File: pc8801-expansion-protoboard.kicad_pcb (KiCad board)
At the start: 2 copper layers, 219 x 95 mm, 42 parts, among them J1 Solder Side, J2 Parts Side, J3 5V, J4 12V, J5 -12V, J6 GND_1, J7 GND_2, U1 ExpansionEdge, U10 74LS165, U11 ESP32-DEVKITC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

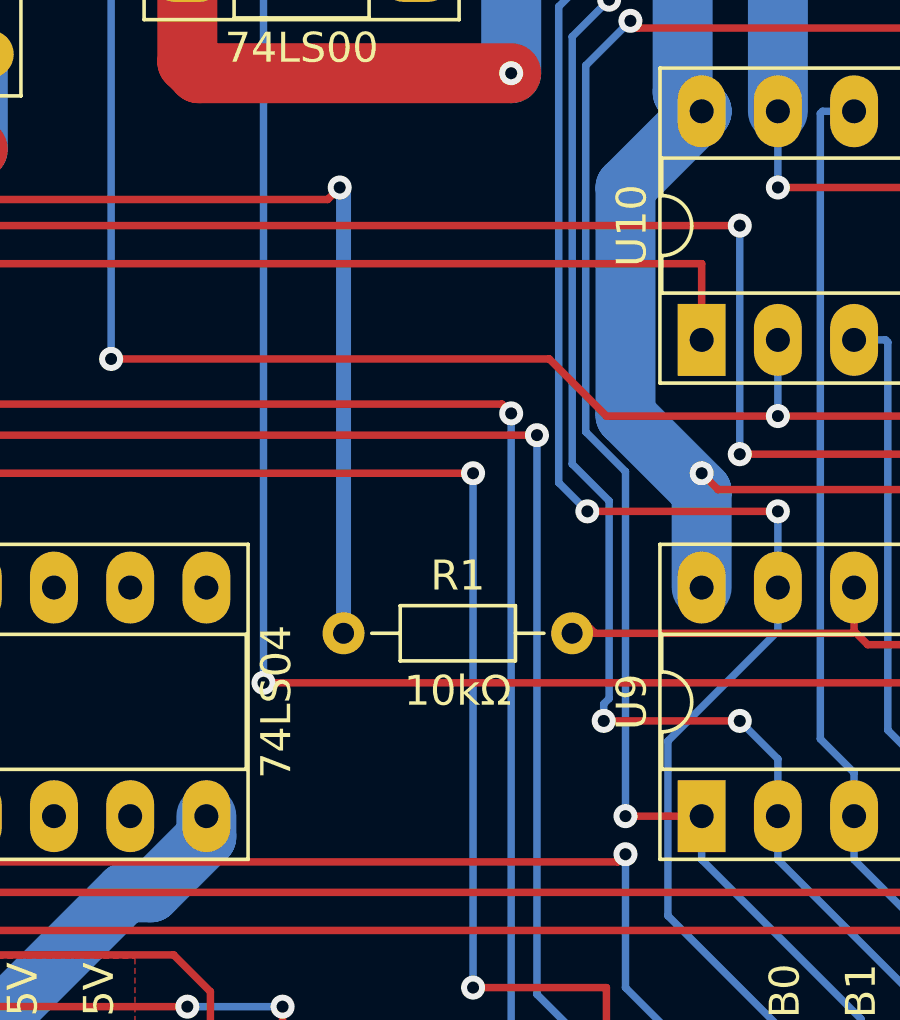
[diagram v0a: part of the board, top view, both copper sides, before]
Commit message: Fix too-tiny R1
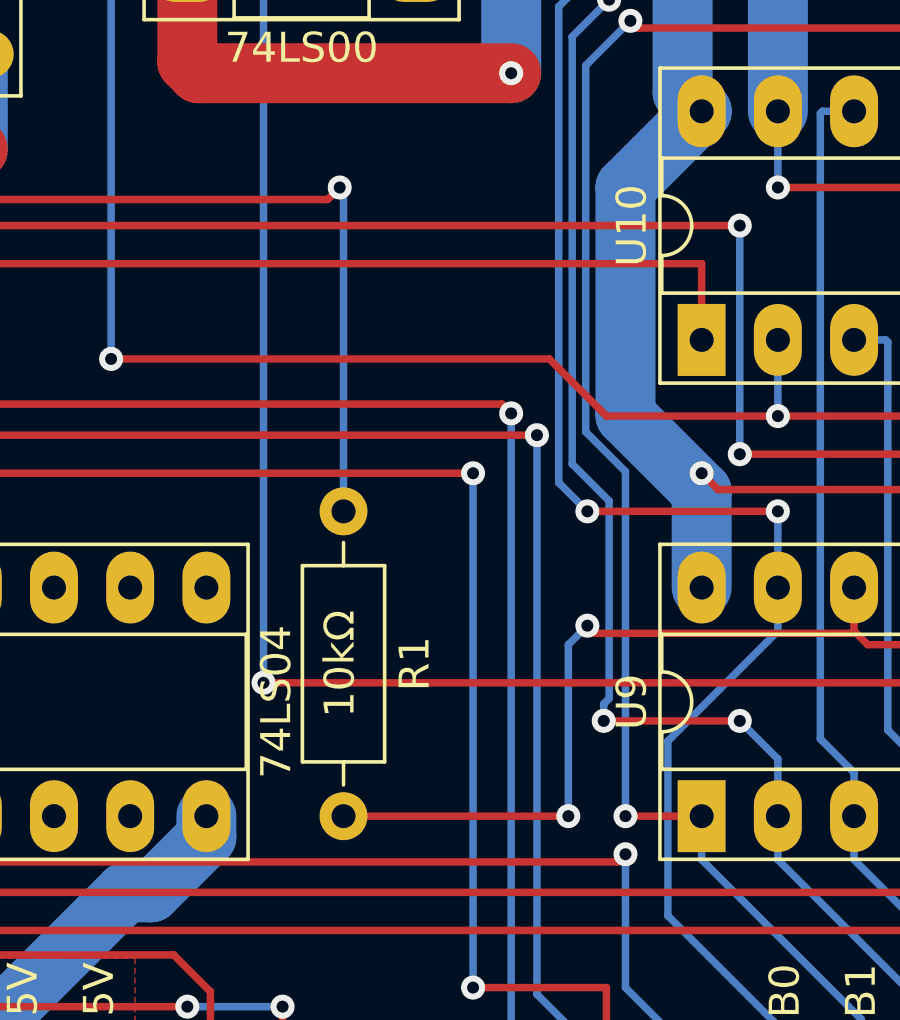
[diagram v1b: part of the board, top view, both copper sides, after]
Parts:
- R1: footprint Resistor_THT:R_Axial_DIN0204_L3.6mm_D1.6mm_P7.62mm_Horizontal -> Resistor_THT:R_Axial_DIN0207_L6.3mm_D2.5mm_P10.16mm_Horizontal
- moved R1 4.06 mm to (124.0, 101.6), turned to -90 degrees
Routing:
- net /FUJI_OUT: track 144.1 -> 158.3 mm, vias 4 -> 6
- net Net-(R1-Pad1): track 82.7 -> 78.7 mm
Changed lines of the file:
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@@
   (net 142 "/SD_MISO")
   (net 143 "unconnected-(X1-Pad1)")
-  (net 144 "Net-(U11-Pad24)")
+  (net 144 "Net-(R3-Pad1)")
   (footprint "PC-8801:1x20_PowerBar" (layer "F.Cu")
     (at 49.53 66.04)
@@
       (net 117 "unconnected-(U11-Pad23)") (pinfunction "IO15") (pintype "bidirectional"))
     (pad "24" thru_hole circle locked (at 12.7 12.71) (size 1.53 1.53) (drill 1.02) (layers *.Cu *.Mask)
-      (net 144 "Net-(U11-Pad24)") (pinfunction "IO2") (pintype "bidirectional"))
+      (net 144 "Net-(R3-Pad1)") (pinfunction "IO2") (pintype "bidirectional"))
     (pad "25" thru_hole circle locked (at 12.7 10.17) (size 1.53 1.53) (drill 1.02) (layers *.Cu *.Mask)
       (net 55 "Net-(R2-Pad1)") (pinfunction "IO0") (pintype "bidirectional"))
@@
       (net 26 "/GND") (pinfunction "GND") (pintype "power_in"))
   )
-  (footprint "Resistor_THT:R_Axial_DIN0204_L3.6mm_D1.6mm_P7.62mm_Horizontal" (layer "F.Cu")
-    (at 123.952 105.664)
-    (descr "Resistor, Axial_DIN0204 series, Axial, Horizontal, pin pitch=7.62mm, 0.167W, length*diameter=3.6*1.6mm^2, http://cdn-reichelt.de/documents/datenblatt/B400/1_4W%23YAG.pdf")
-    (tags "Resistor Axial_DIN0204 series Axial Horizontal pin pitch 7.62mm 0.167W length 3.6mm diameter 1.6mm")
+  (footprint "Resistor_THT:R_Axial_DIN0207_L6.3mm_D2.5mm_P10.16mm_Horizontal" (layer "F.Cu")
+    (at 123.952 101.6 -90)
+    (descr "Resistor, Axial_DIN0207 series, Axial, Horizontal, pin pitch=10.16mm, 0.25W = 1/4W, length*diameter=6.3*2.5mm^2, http://cdn-reichelt.de/documents/datenblatt/B400/1_4W%23YAG.pdf")
+    (tags "Resistor Axial_DIN0207 series Axial Horizontal pin pitch 10.16mm 0.25W = 1/4W length 6.3mm diameter 2.5mm")
     (property "Sheetfile" "pc8801-expansion-protoboard.kicad_sch")
     (property "Sheetname" "")
     (attr through_hole)
-    (fp_text reference "R1" (at 3.81 -1.92) (layer "F.SilkS")
+    (fp_text reference "R1" (at 5.08 -2.37 90) (layer "F.SilkS")
       (effects (font (size 1 1) (thickness 0.15)))
     )
-    (fp_text value "10kΩ" (at 3.81 1.92) (layer "F.SilkS")
+    (fp_text value "10kΩ" (at 5.08 0.127 90) (layer "F.SilkS")
       (effects (font (size 1 1) (thickness 0.15)))
     )
-    (fp_text user "${REFERENCE}" (at 3.81 0) (layer "F.Fab")
-      (effects (font (size 0.72 0.72) (thickness 0.108)))
+    (fp_text user "${REFERENCE}" (at 5.08 0 90) (layer "F.Fab")
+      (effects (font (size 1 1) (thickness 0.15)))
     )
-    (fp_line (start 6.68 0) (end 5.73 0) (layer "F.SilkS") (width 0.12))
-    (fp_line (start 0.94 0) (end 1.89 0) (layer "F.SilkS") (width 0.12))
-    (fp_line (start 1.89 0.92) (end 5.73 0.92) (layer "F.SilkS") (width 0.12))
-    (fp_line (start 5.73 -0.92) (end 1.89 -0.92) (layer "F.SilkS") (width 0.12))
-    (fp_line (start 1.89 -0.92) (end 1.89 0.92) (layer "F.SilkS") (width 0.12))
-    (fp_line (start 5.73 0.92) (end 5.73 -0.92) (layer "F.SilkS") (width 0.12))
-    (fp_line (start 8.57 -1.05) (end -0.95 -1.05) (layer "F.CrtYd") (width 0.05))
-    (fp_line (start 8.57 1.05) (end 8.57 -1.05) (layer "F.CrtYd") (width 0.05))
-    (fp_line (start -0.95 -1.05) (end -0.95 1.05) (layer "F.CrtYd") (width 0.05))
-    (fp_line (start -0.95 1.05) (end 8.57 1.05) (layer "F.CrtYd") (width 0.05))
-    (fp_line (start 2.01 -0.8) (end 2.01 0.8) (layer "F.Fab") (width 0.1))
-    (fp_line (start 5.61 -0.8) (end 2.01 -0.8) (layer "F.Fab") (width 0.1))
-    (fp_line (start 7.62 0) (end 5.61 0) (layer "F.Fab") (width 0.1))
-    (fp_line (start 5.61 0.8) (end 5.61 -0.8) (layer "F.Fab") (width 0.1))
-    (fp_line (start 2.01 0.8) (end 5.61 0.8) (layer "F.Fab") (width 0.1))
-    (fp_line (start 0 0) (end 2.01 0) (layer "F.Fab") (width 0.1))
-    (pad "1" thru_hole circle (at 0 0) (size 1.4 1.4) (drill 0.7) (layers *.Cu *.Mask)
+    (fp_line (start 1.81 1.37) (end 8.35 1.37) (layer "F.SilkS") (width 0.12))
+    (fp_line (start 9.12 0) (end 8.35 0) (layer "F.SilkS") (width 0.12))
+    (fp_line (start 8.35 1.37) (end 8.35 -1.37) (layer "F.SilkS") (width 0.12))
+    (fp_line (start 8.35 -1.37) (end 1.81 -1.37) (layer "F.SilkS") (width 0.12))
+    (fp_line (start 1.04 0) (end 1.81 0) (layer "F.SilkS") (width 0.12))
+    (fp_line (start 1.81 -1.37) (end 1.81 1.37) (layer "F.SilkS") (width 0.12))
+    (fp_line (start 11.21 -1.5) (end -1.05 -1.5) (layer "F.CrtYd") (width 0.05))
+    (fp_line (start -1.05 1.5) (end 11.21 1.5) (layer "F.CrtYd") (width 0.05))
+    (fp_line (start -1.05 -1.5) (end -1.05 1.5) (layer "F.CrtYd") (width 0.05))
+    (fp_line (start 11.21 1.5) (end 11.21 -1.5) (layer "F.CrtYd") (width 0.05))
+    (fp_line (start 1.93 -1.25) (end 1.93 1.25) (layer "F.Fab") (width 0.1))
+    (fp_line (start 10.16 0) (end 8.23 0) (layer "F.Fab") (width 0.1))
+    (fp_line (start 0 0) (end 1.93 0) (layer "F.Fab") (width 0.1))
+    (fp_line (start 8.23 1.25) (end 8.23 -1.25) (layer "F.Fab") (width 0.1))
+    (fp_line (start 1.93 1.25) (end 8.23 1.25) (layer "F.Fab") (width 0.1))
+    (fp_line (start 8.23 -1.25) (end 1.93 -1.25) (layer "F.Fab") (width 0.1))
+    (pad "1" thru_hole circle (at 0 0 270) (size 1.6 1.6) (drill 0.8) (layers *.Cu *.Mask)
       (net 72 "Net-(R1-Pad1)") (pintype "passive"))
-    (pad "2" thru_hole oval (at 7.62 0) (size 1.4 1.4) (drill 0.7) (layers *.Cu *.Mask)
+    (pad "2" thru_hole oval (at 10.16 0 270) (size 1.6 1.6) (drill 0.8) (layers *.Cu *.Mask)
       (net 71 "/FUJI_OUT") (pintype "passive"))
-    (model "${KICAD6_3DMODEL_DIR}/Resistor_THT.3dshapes/R_Axial_DIN0204_L3.6mm_D1.6mm_P7.62mm_Horizontal.wrl"
+    (model "${KICAD6_3DMODEL_DIR}/Resistor_THT.3dshapes/R_Axial_DIN0207_L6.3mm_D2.5mm_P10.16mm_Horizontal.wrl"
       (offset (xyz 0 0 0))
       (scale (xyz 1 1 1))
@@
     (fp_line (start 1.93 1.25) (end 8.23 1.25) (layer "F.Fab") (width 0.1))
     (pad "1" thru_hole circle (at 0 0 270) (size 1.6 1.6) (drill 0.8) (layers *.Cu *.Mask)
-      (net 144 "Net-(U11-Pad24)") (pintype "passive"))
+      (net 144 "Net-(R3-Pad1)") (pintype "passive"))
     (pad "2" thru_hole oval (at 10.16 0 270) (size 1.6 1.6) (drill 0.8) (layers *.Cu *.Mask)
       (net 116 "Net-(D2-Pad2)") (pintype "passive"))
@@
   (segment (start 156.83 71.135) (end 156.845 71.12) (width 0.5) (layer "F.Cu") (net 71))
   (segment (start 154.305 71.135) (end 156.83 71.135) (width 0.5) (layer "F.Cu") (net 71))
+  (segment (start 123.952 111.76) (end 131.445 111.76) (width 0.25) (layer "F.Cu") (net 71))
   (segment (start 158.115 105.41) (end 157.48 106.045) (width 0.25) (layer "F.Cu") (net 71))
   (segment (start 141.425 106.045) (end 140.97 105.59) (width 0.25) (layer "F.Cu") (net 71))
+  (segment (start 132.08 105.41) (end 132.33501 105.66501) (width 0.25) (layer "F.Cu") (net 71))
   (segment (start 140.89499 105.66501) (end 132.33501 105.66501) (width 0.25) (layer "F.Cu") (net 71))
   (segment (start 157.48 106.045) (end 141.425 106.045) (width 0.25) (layer "F.Cu") (net 71))
   (segment (start 212.09 105.41) (end 158.115 105.41) (width 0.25) (layer "F.Cu") (net 71))
   (segment (start 140.97 105.59) (end 140.89499 105.66501) (width 0.25) (layer "F.Cu") (net 71))
-  (segment (start 132.33501 105.66501) (end 132.144999 105.474999) (width 0.25) (layer "F.Cu") (net 71))
   (segment (start 210.82 83.82) (end 212.09 83.82) (width 0.25) (layer "F.Cu") (net 71))
   (via (at 212.09 105.41) (size 0.8) (drill 0.4) (layers "F.Cu" "B.Cu") (net 71))
+  (via (at 131.445 111.76) (size 0.8) (drill 0.4) (layers "F.Cu" "B.Cu") (net 71))
   (via (at 156.845 106.045) (size 0.8) (drill 0.4) (layers "F.Cu" "B.Cu") (net 71))
   (via (at 156.845 71.12) (size 0.8) (drill 0.4) (layers "F.Cu" "B.Cu") (net 71))
   (via (at 212.09 83.82) (size 0.8) (drill 0.4) (layers "F.Cu" "B.Cu") (net 71))
+  (via (at 132.08 105.41) (size 0.8) (drill 0.4) (layers "F.Cu" "B.Cu") (net 71))
+  (segment (start 131.445 106.045) (end 132.08 105.41) (width 0.25) (layer "B.Cu") (net 71))
+  (segment (start 131.445 111.76) (end 131.445 106.045) (width 0.25) (layer "B.Cu") (net 71))
   (segment (start 212.09 105.41) (end 209.849489 103.169489) (width 0.25) (layer "B.Cu") (net 71))
   (segment (start 209.849489 86.060511) (end 212.09 83.82) (width 0.25) (layer "B.Cu") (net 71))
@@
   (via (at 99.695 86.36) (size 0.8) (drill 0.4) (layers "F.Cu" "B.Cu") (net 72))
   (via (at 76.2 86.36) (size 0.8) (drill 0.4) (layers "F.Cu" "B.Cu") (net 72))
-  (segment (start 123.952 90.932) (end 123.825 90.805) (width 0.5) (layer "B.Cu") (net 72))
+  (segment (start 123.952 90.932) (end 123.952 101.6) (width 0.25) (layer "B.Cu") (net 72))
   (segment (start 76.2 86.36) (end 76.2 83.82) (width 0.25) (layer "B.Cu") (net 72))
   (segment (start 99.695 86.36) (end 99.695 91.13501) (width 0.25) (layer "B.Cu") (net 72))
   (segment (start 66.04 83.82) (end 66.04 86.36) (width 0.25) (layer "B.Cu") (net 72))
-  (segment (start 123.952 105.664) (end 123.952 90.932) (width 0.5) (layer "B.Cu") (net 72))
+  (segment (start 123.825 90.805) (end 123.952 90.932) (width 0.25) (layer "B.Cu") (net 72))
   (segment (start 111.76 71.12) (end 113.21 71.12) (width 0.25) (layer "F.Cu") (net 74))
   (segment (start 126.28999 69.99499) (end 126.365 70.07) (width 0.25) (layer "F.Cu") (net 74))

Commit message: Bump version
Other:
- board text added: "Easter Island"
- board text added: "v0.4 leadedsolder.com 2021-2022"
- board text removed: "Whoops ]["
- board text removed: "v0.3 leadedsolder.com 2021-2022"
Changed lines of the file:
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@@
     (effects (font (size 1 1) (thickness 0.15)))
   )
-  (gr_text "v0.3 leadedsolder.com 2021-2022" (at 49 58) (layer "F.SilkS")
+  (gr_text "v0.4 leadedsolder.com 2021-2022" (at 49 58) (layer "F.SilkS")
     (effects (font (size 2 2) (thickness 0.15)) (justify left))
   )
@@
     (effects (font (size 1 1) (thickness 0.15)))
   )
-  (gr_text "Whoops ][" (at 72.39 125.095) (layer "F.SilkS")
+  (gr_text "Easter Island" (at 72.39 125.095) (layer "F.SilkS")
     (effects (font (size 4 4) (thickness 1) italic))
   )

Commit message: reset button
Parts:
- added SW1: Reset ESP, Button_Switch_THT:SW_PUSH_6mm, F.Cu at (137.7, 57.7)
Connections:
- net /GND renamed GND
- U11 pad 2: unconnected-(U11-Pad2) -> /~{ESP_RESET}
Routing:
- net /~{ESP_RESET}: track 0.00 -> 54.6 mm, vias 0 -> 4

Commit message: Add bypass caps for counter and ESP
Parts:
- added C3: 0.1µF, Capacitor_THT:C_Disc_D5.0mm_W2.5mm_P2.50mm, F.Cu at (166.8, 98.5)
- added C4: 0.1µF, Capacitor_THT:C_Disc_D5.0mm_W2.5mm_P2.50mm, F.Cu at (101.0, 83.5)
- moved D1 32.7 mm to (225.3, 68.0)
- moved R2 32.1 mm to (216.0, 78.2)
- moved D2 31.9 mm to (225.2, 75.0)
- moved R3 20.3 mm to (219.2, 83.6), turned to 90 degrees
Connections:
- R3 pad 1: Net-(R3-Pad1) -> Net-(U11-Pad33)
- U11 pad 24: Net-(R3-Pad1) -> unconnected-(U11-Pad24)
- U11 pad 25: Net-(R2-Pad1) -> unconnected-(U11-Pad25)
- U11 pad 33: unconnected-(U11-Pad33) -> Net-(U11-Pad33)
- U11 pad 36: unconnected-(U11-Pad36) -> Net-(R2-Pad1)
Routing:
- net GND: track 462.7 -> 426.7 mm, vias 16 -> 15
- net Net-(U11-Pad33): track 0.00 -> 19.3 mm, vias 0 -> 2
- net Net-(R3-Pad1): track 6.81 -> 0.00 mm
- net Net-(R2-Pad1): track 12.8 -> 18.9 mm, vias 1 -> 2
- net /+5V: track 423.6 -> 427.9 mm
- net Net-(R2-Pad2): track 3.05 -> 6.75 mm
- net Net-(D2-Pad2): track 7.66 -> 4.11 mm
- net /~{FUJI_CS}: track 209.1 -> 209.9 mm

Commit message: Fix up DRC
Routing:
- net /~{ESP_RESET}: track 54.6 -> 61.1 mm
- net /~{START}: track 72.8 -> 73.7 mm
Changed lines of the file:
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@@
   (segment (start 138.67 75.17) (end 138.43 74.93) (width 1) (layer "F.Cu") (net 26))
   (segment (start 103.451559 86.36) (end 100.911559 83.82) (width 2) (layer "F.Cu") (net 26))
+  (segment (start 179.000489 99.000489) (end 156.289511 99.000489) (width 2) (layer "F.Cu") (net 26))
   (segment (start 148.64 75.17) (end 138.67 75.17) (width 1) (layer "F.Cu") (net 26))
   (segment (start 78.74 83.82) (end 96.52 83.82) (width 2) (layer "F.Cu") (net 26))
   (segment (start 221.615 114.3) (end 223.52 114.3) (width 2) (layer "F.Cu") (net 26))
+  (segment (start 156.289511 99.000489) (end 156.22 99.07) (width 2) (layer "F.Cu") (net 26))
+  (segment (start 179.07 99.07) (end 179.000489 99.000489) (width 2) (layer "F.Cu") (net 26))
   (segment (start 160.578 66.09) (end 160.75 66.262) (width 0.5) (layer "F.Cu") (net 26))
   (segment (start 223.52 114.3) (end 225.425 112.395) (width 2) (layer "F.Cu") (net 26))
@@
   (segment (start 119.12 86.995) (end 129.54 86.995) (width 2) (layer "F.Cu") (net 26))
   (segment (start 156.875224 66.09) (end 160.578 66.09) (width 0.5) (layer "F.Cu") (net 26))
-  (segment (start 179.07 99.07) (end 156.22 99.07) (width 2) (layer "F.Cu") (net 26))
   (segment (start 118.745 86.62) (end 119.12 86.995) (width 2) (layer "F.Cu") (net 26))
   (segment (start 97.085685 83.82) (end 96.52 83.82) (width 2) (layer "F.Cu") (net 26))
@@
   (segment (start 126.365 83.82) (end 124.915 83.82) (width 0.25) (layer "B.Cu") (net 76))
   (segment (start 126.365 76.2) (end 118.745 76.2) (width 0.25) (layer "F.Cu") (net 77))
-  (segment (start 123.645 80.01) (end 72.39 80.01) (width 0.25) (layer "F.Cu") (net 78))
-  (segment (start 126.365 78.74) (end 124.915 78.74) (width 0.25) (layer "F.Cu") (net 78))
-  (segment (start 123.645 80.01) (end 124.915 78.74) (width 0.25) (layer "F.Cu") (net 78))
+  (segment (start 93.6597 80.01) (end 96.054211 77.615489) (width 0.25) (layer "F.Cu") (net 78))
+  (segment (start 72.39 80.01) (end 93.6597 80.01) (width 0.25) (layer "F.Cu") (net 78))
+  (segment (start 96.054211 77.615489) (end 125.240489 77.615489) (width 0.25) (layer "F.Cu") (net 78))
+  (segment (start 125.240489 77.615489) (end 126.365 78.74) (width 0.25) (layer "F.Cu") (net 78))
   (via (at 72.39 80.01) (size 0.8) (drill 0.4) (layers "F.Cu" "B.Cu") (net 78))
   (segment (start 71.12 95.25) (end 71.12 97.79) (width 0.25) (layer "B.Cu") (net 78))
@@
   (segment (start 179.07 68.59) (end 171.05 68.59) (width 0.25) (layer "F.Cu") (net 88))
   (segment (start 170.83 61.06) (end 158.342 61.06) (width 0.25) (layer "F.Cu") (net 88))
+  (segment (start 137.668 53.158) (end 141.152 56.642) (width 0.25) (layer "F.Cu") (net 88))
   (segment (start 158.242 56.642) (end 141.152 56.642) (width 0.25) (layer "F.Cu") (net 88))
+  (segment (start 131.168 53.158) (end 137.668 53.158) (width 0.25) (layer "F.Cu") (net 88))
   (segment (start 158.342 61.06) (end 158.242 60.96) (width 0.25) (layer "F.Cu") (net 88))
-  (segment (start 141.152 56.642) (end 137.668 53.158) (width 0.25) (layer "F.Cu") (net 88))
   (segment (start 171.05 68.59) (end 171 68.54) (width 0.25) (layer "F.Cu") (net 88))
   (via (at 171 68.54) (size 0.8) (drill 0.4) (layers "F.Cu" "B.Cu") (net 88))
